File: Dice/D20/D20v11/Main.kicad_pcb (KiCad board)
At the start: 2 copper layers, 77.5 x 48.1 mm, 108 parts, among them J1 Conn_01x14, J2 Conn_01x11, J3 Conn_01x02, P5 COILA, P6 COILB, U1 N52810_QFN32, U2 MXC400xXC, U3 HX6306P502MR, U4 LN3406, U5 MCP73832T-2ACI/OT, U6 MT9700, U7 74AHC1G08, U8 TMR1366, Y1 32MHz 40ppm

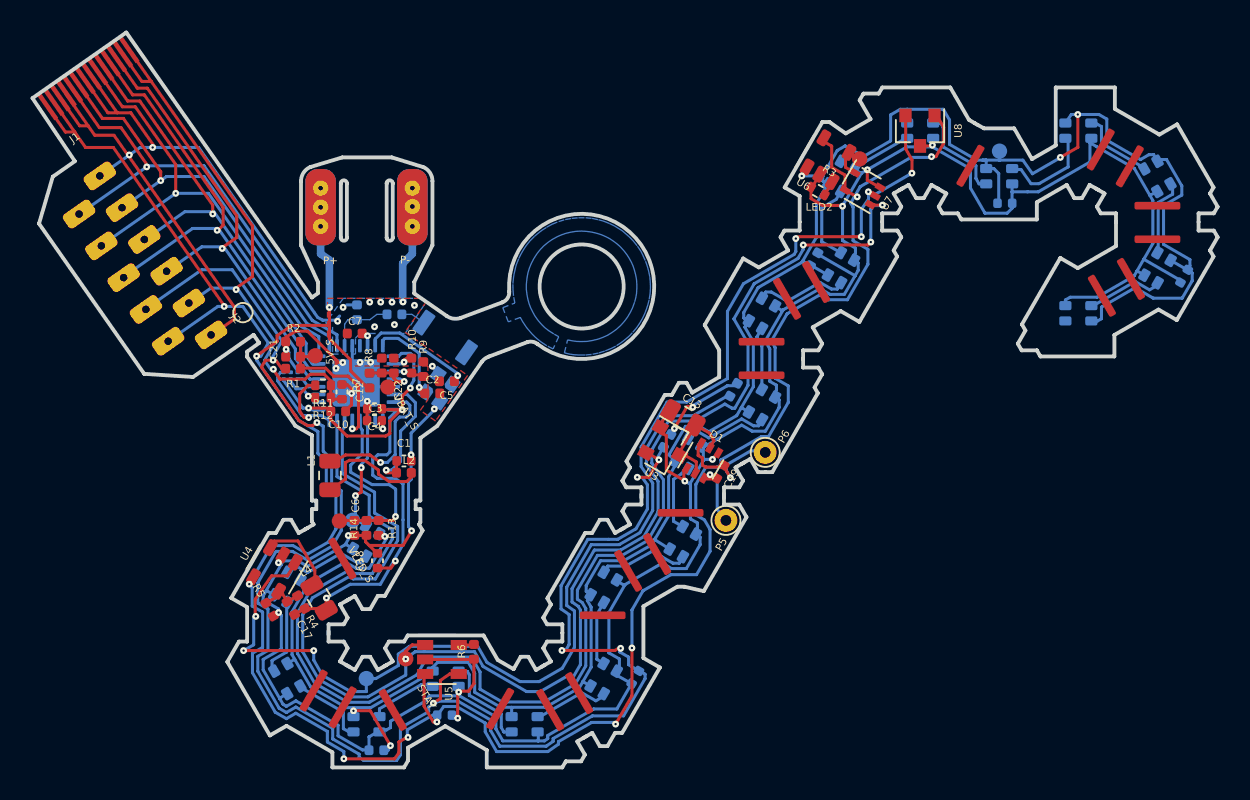
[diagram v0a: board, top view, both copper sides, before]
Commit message: Added Dice V11 boards and several other projects, including new Charger designs, Adaptor boards and JIGs
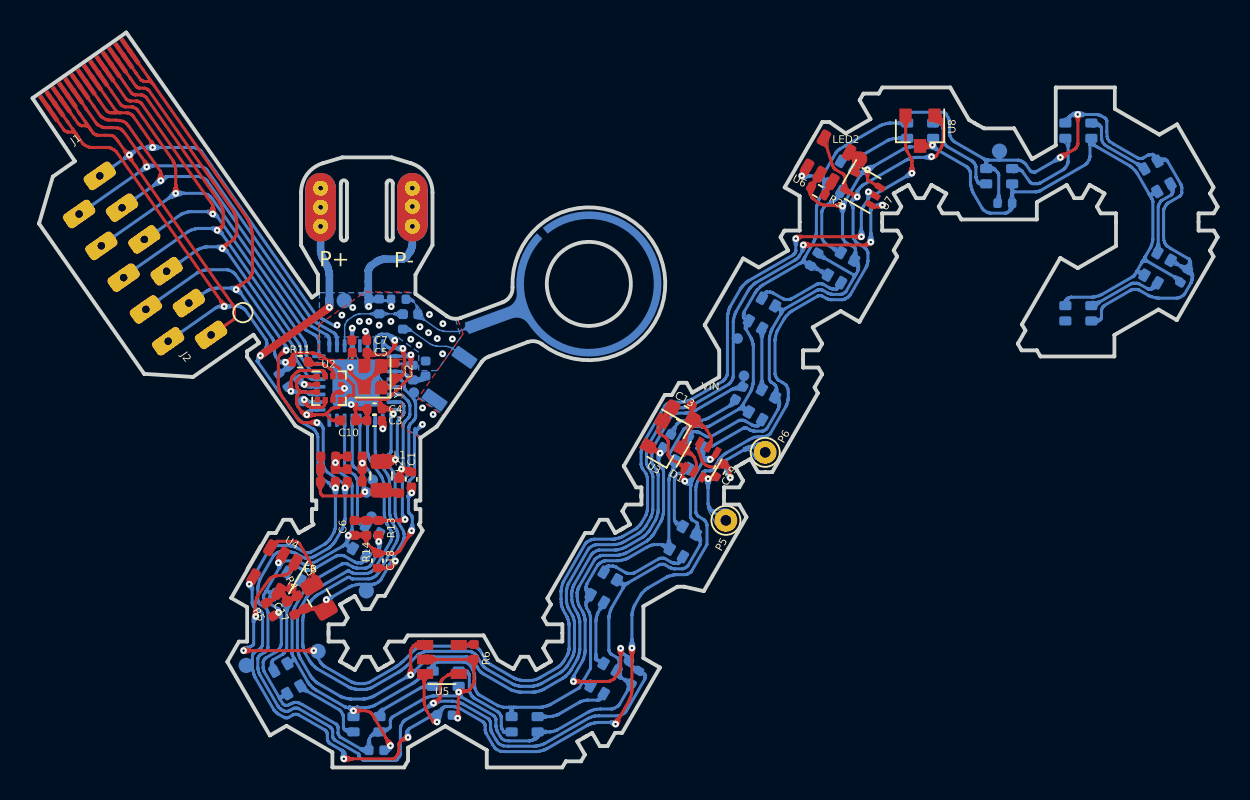
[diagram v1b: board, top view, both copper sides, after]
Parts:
- removed C12: 4.7uF 6.3V 20%, Capacitor_SMD:C_0402_1005Metric
- removed REF** (x22): Stiffener, Pixels-dice:Stiffener
- added AE2: ARC, Pixels-dice:ARC_Antenna, B.Cu at (148.5, 85.0)
- added C11: DNP, Capacitor_SMD:C_0402_1005Metric, B.Cu at (144.5, 82.9)
- added L5: DNP, Inductor_SMD:L_0402_1005Metric, B.Cu at (145.2, 83.9)
- added R16: 2.7k 5%, Resistor_SMD:R_0402_1005Metric, B.Cu at (137.6, 87.7)
- added W14: BATT, Pixels-dice:TEST_PIN, B.Cu at (134.5, 106.9)
- added W15: +5V, Pixels-dice:TEST_PIN, B.Cu at (159.6, 106.6)
- added W16: VIN, Pixels-dice:TEST_PIN, F.Cu at (163.6, 89.9)
- added W18: FB, Pixels-dice:TEST_PIN, F.Cu at (137.5, 101.8)
- added W19: GND, Pixels-dice:TEST_PIN, B.Cu at (140.9, 83.0)
- added W25: VDD, Pixels-dice:TEST_PIN, B.Cu at (142.4, 102.0)
- added W5: LED_EN, Pixels-dice:TEST_PIN, B.Cu at (166.7, 85.5)
- added W7: ACC_INT, Pixels-dice:TEST_PIN, B.Cu at (138.2, 89.6)
- AE1: value Antenna -> Chip
- C13: footprint Capacitor_SMD:C_0805_2012Metric -> Capacitor_SMD:C_0603_1608Metric
- C19: value 500pF 50V 10% -> 82nF 50V 10%
- R1, R13, R7: value 4M 1% -> 4.02M 1%
- R10, R12, W12, W13, W17, W20: moved to B.Cu
- R11: value 2.7k 5% -> 0 Ohm
- R3: value 68k 5% -> 10k 5%
- R9: value 82.5K 1% -> 100k 1%; moved to B.Cu
- U2: value MXC400xXC -> KXTJ3-1057; footprint Pixels-dice:WLP-6 -> Package_LGA:LGA-12_2x2mm_P0.5mm; moved to F.Cu
- Y1: moved to F.Cu
- moved W17 28.9 mm to (167.1, 87.9)
- moved W12 9.71 mm to (145.5, 89.0)
- moved R2 9.26 mm to (141.6, 94.1)
- moved W13 8.95 mm to (142.8, 94.8)
- moved R1 8.43 mm to (141.6, 94.9)
- moved C22 8.03 mm to (139.9, 94.0), turned to 0 degrees
- moved C21 7.68 mm to (141.6, 93.2)
- moved R7 7.16 mm to (139.8, 94.9), turned to 180 degrees
- moved W20 7.03 mm to (142.4, 95.6)
- moved R8 6.90 mm to (139.9, 93.2), turned to 0 degrees
- moved C5 6.01 mm to (141.9, 86.4)
- moved Y1 4.38 mm to (142.8, 88.0), turned to 90 degrees
- moved W23 3.63 mm to (139.2, 106.0)
- moved AE1 3.49 mm to (148.8, 86.7), turned to 325 degrees
- moved L1 3.35 mm to (143.3, 94.5)
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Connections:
- net /ANTENNA renamed /CHIP_ANTENNA
- AE1 pad 2: Net-(AE1-Pad2) -> (no net)
- D21 pad 3: Net-(D21-Pad3) -> (no net)
- R11 pad 1: VDD -> Net-(R11-Pad1)
- R11 pad 2: /SCL -> VDD
- R12 pad 2: /SDA -> /SCL
- U1 pad 10: Net-(U1-Pad10) -> /ACC_INT
- U1 pad 11: /SDA -> /SCL
- U1 pad 12: /ACC_INT -> /SDA
- U1 pad 2: Net-(U1-Pad2) -> /LED_EN
- U1 pad 21: Net-(U1-Pad21) -> (no net)
- U1 pad 28: /VBAT_SENSE -> /VLED_SENSE
- U1 pad 3: /LED_DATA -> /STATS
- U1 pad 4: /VLED_SENSE -> /5V_SENSE
- U1 pad 5: /5V_SENSE -> /VBAT_SENSE
- U1 pad 6: /STATS -> /LED_DATA
- U1 pad 7: /LED_EN -> (no net)
- U1 pad 8: /SCL -> (no net)
- U2 pad 1: /SCL -> VDD
- U2 pad 2: Net-(U2-Pad2) -> /SDA
- U2 pad 3: GND -> VDD
- U2 pad 4: /ACC_INT -> (no net)
- U2 pad 5: /SDA -> /ACC_INT
- U2 pad 6: VDD -> GND
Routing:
- net GND: track 262.8 -> 311.3 mm, vias 32 -> 40
- net /VBAT_SENSE: track 4.15 -> 14.8 mm
- net VDD: track 79.9 -> 89.6 mm
- net VBAT: track 175.6 -> 183.6 mm, vias 11 -> 12
- net /LED_EN: track 92.0 -> 86.0 mm
- net +5V: track 108.3 -> 114.2 mm
- net /VLED_SENSE: track 12.6 -> 18.3 mm
- net /Power/MAG1_: track 86.1 -> 90.8 mm
- net /ARC_ANTENNA: track 0.00 -> 4.41 mm
- net VLED: track 153.7 -> 157.8 mm
- net Net-(L1-Pad1): track 9.77 -> 13.8 mm
- net Net-(C3-Pad1): track 1.11 -> 5.06 mm
- net Net-(L1-Pad2): track 7.68 -> 3.79 mm
- net Net-(R11-Pad1): track 0.00 -> 3.59 mm
- net RESET: track 31.5 -> 34.4 mm
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- removed copper zone on B.Cu, net (none)
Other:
- outline, holes or cut-outs redrawn
- net class Antenna: trace_width 0.08 -> 0.09
- board text added: "PIXELS D20 V11 PCB SYSTEMIC GAMES"
- board text removed: "PIXELS D20 V10 PCB SYSTEMIC GAMES"

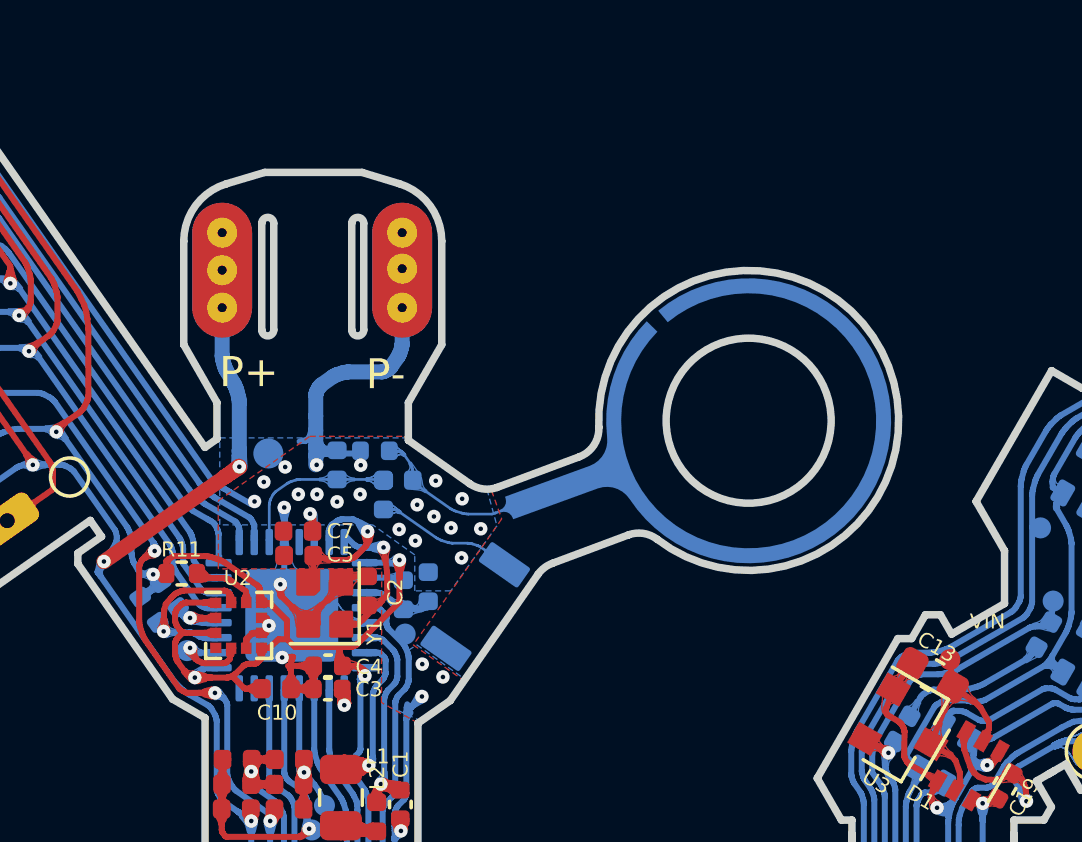
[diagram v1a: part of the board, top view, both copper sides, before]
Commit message: Upgraded a number of projects to Kicad V6 and added D6, PD6 and D12
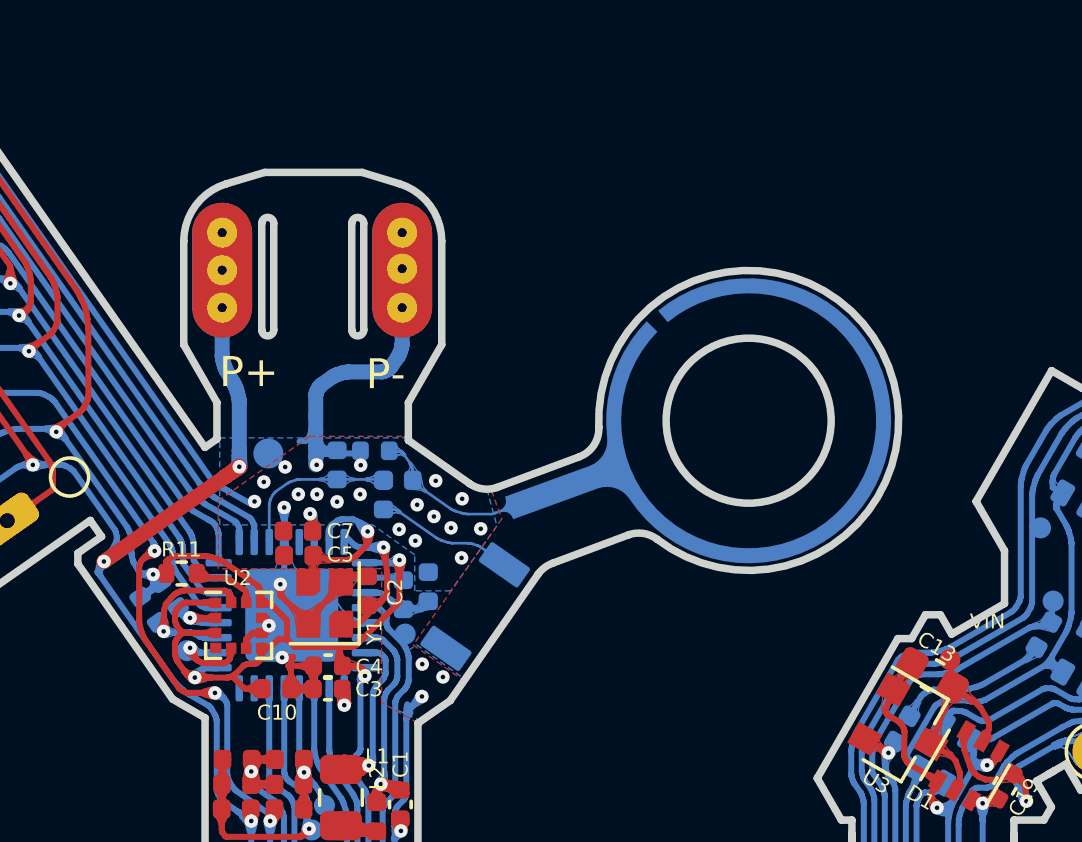
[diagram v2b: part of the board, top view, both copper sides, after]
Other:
- net class Antenna removed
- net class Default removed
